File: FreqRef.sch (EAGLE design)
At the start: 33 parts, among them J1 ISP Connector, J2 BNC_RIGHT-ANGLE, SW1 PWR, U1 ATMEGA328, U2 MIC5205, U3 SN74LV164APW

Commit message: Start of Rev-B
Change name to FrequencyReference.
Added part num to BNC connector.
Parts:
- FRAME1: CREVISION Rev A -> Rev B; DATECODE 02SEP2015 -> 2015
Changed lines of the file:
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@@
 <part name="FRAME1" library="NewFrame" deviceset="FRAME_LTR_CU_MARK" device="">
 <attribute name="CNAME" value="Frequency Standard"/>
-<attribute name="CREVISION" value="Rev A"/>
-<attribute name="DATECODE" value="02SEP2015"/>
+<attribute name="CREVISION" value="Rev B"/>
+<attribute name="DATECODE" value="2015"/>
 <attribute name="DESIGNER" value="C.Schnarel"/>
 </part>

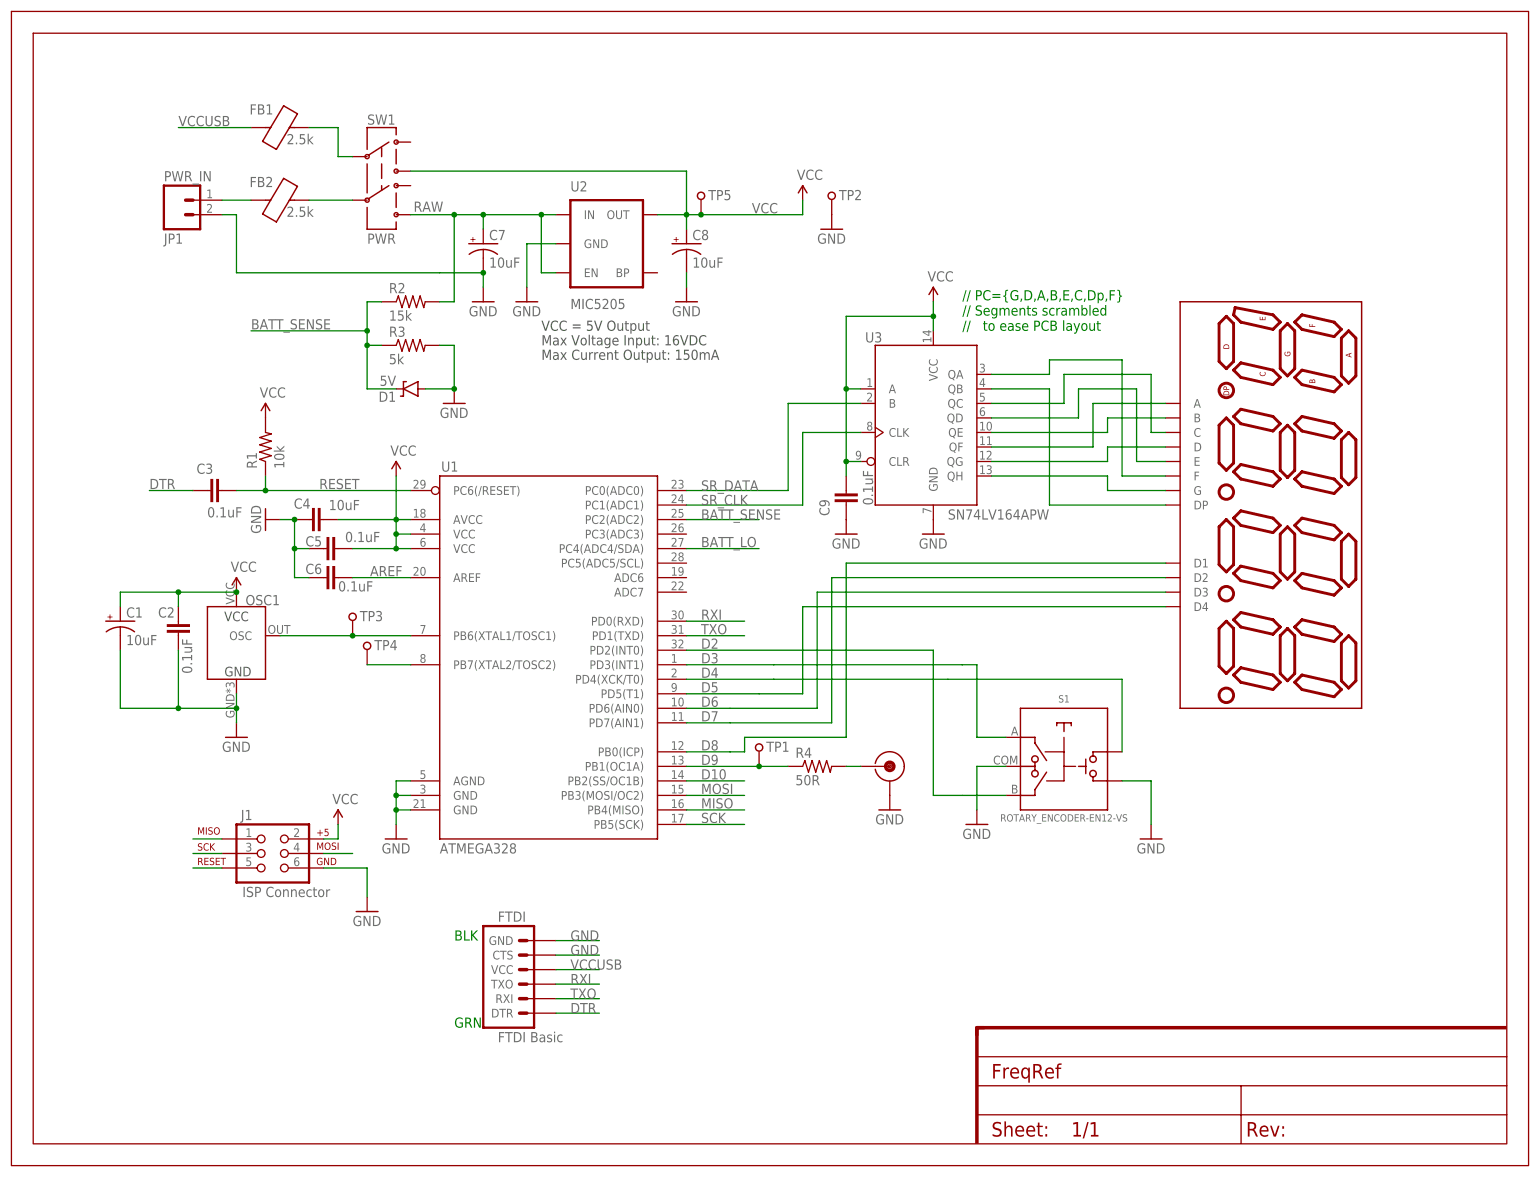
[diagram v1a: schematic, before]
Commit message: More docs. Rev-B layout. Debugged sketch.
Continue documentation. Added two oscillator options to PCB schematic
and layout.  Debugged sketch  on Redboard.
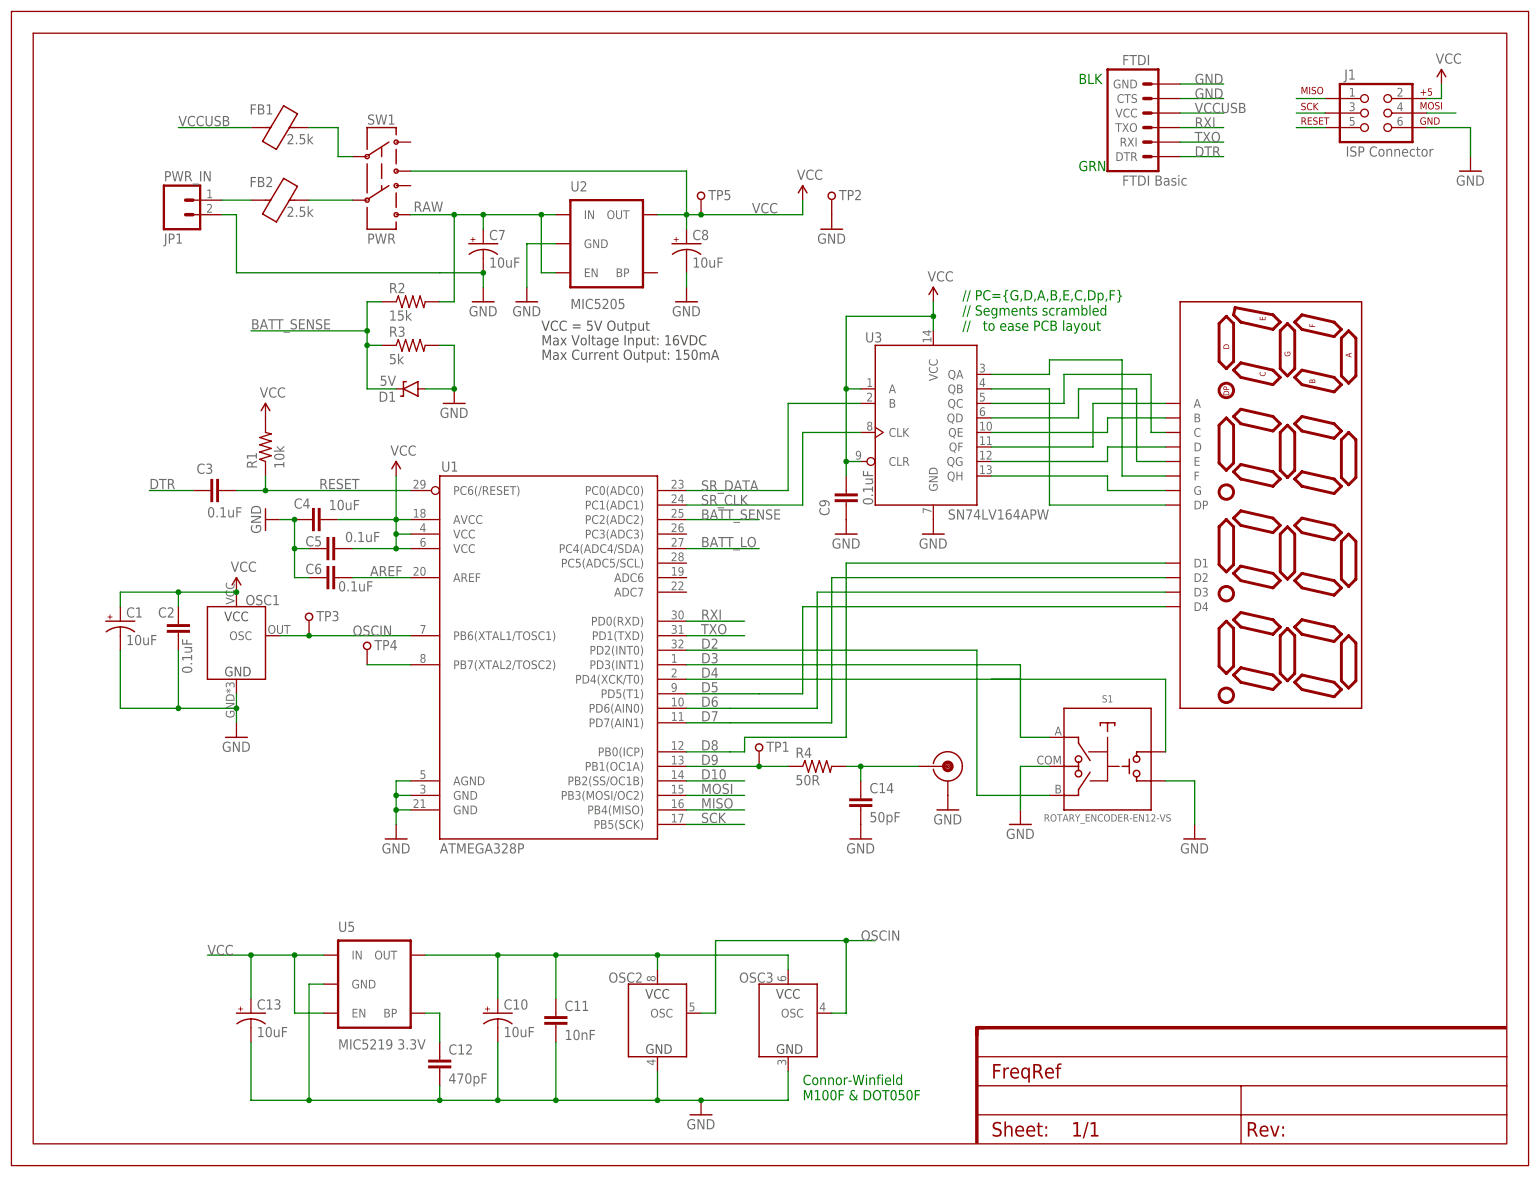
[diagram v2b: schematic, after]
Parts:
- added C10, C13: 10uF, ChipsParts:CAP_POL0805
- added C11: 10nF, SparkFun-Capacitors:CAP0805
- added C12: 470pF, SparkFun-Capacitors:CAP0805
- added C14: 50pF, SparkFun-Capacitors:CAP0805
- added OSC2: (no value), playground:TCXOM100
- added OSC3: (no value), playground:TCXODOT
- added U5: MIC5219 3.3V, SparkFun-PowerIC:V_REG_MIC52193.3V
- FRAME1: CNAME Frequency Standard -> Frequency Reference; CREVISION Rev B -> Rev-B
- OSC1: device playground:TCXO-RTXO230LC -> playground:TCXORALTRON
- U1: value ATMEGA328 -> ATMEGA328P
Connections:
- net N$31 renamed VIN
- removed net N$5: OSC1.OSC, TP3.P$1, U1.PB6(XTAL1/TOSC1)
- new net N$14: C10.+, C11.1, OSC2.VCC, OSC3.VCC, U5.OUT
- new net N$15: C12.1, U5.BP
- new net OSCIN: OSC1.OSC, OSC2.OSC, OSC3.OSC, TP3.P$1, U1.PB6(XTAL1/TOSC1)
- net GND: now also C10.-, C11.2, C12.2, C13.-, C14.2, OSC2.GND, OSC3.GND, U5.GND
- net N$11: now also C14.1
- net VCC: now also C13.+, U5.EN, U5.IN
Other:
- note added: "Connor-Winfield M100F & DOT050F"
- moved on the sheet: FTDI, J1, S1, TP3

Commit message: Software debug.  Schematic values. Added photos.
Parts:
- R2: value 15k -> 10k
- R3: value 5k -> 3.3k
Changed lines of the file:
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@@
 <part name="JP1" library="SparkFun-Connectors" deviceset="M02" device="POLAR" value="PWR_IN"/>
 <part name="SW1" library="StdBxLibrary_BETA_" deviceset="SWITCH,BUTTON,ROUND,7MM" device="" value="PWR"/>
-<part name="R2" library="SparkFun-Resistors" deviceset="RESISTOR" device="0805-RES" value="15k"/>
-<part name="R3" library="SparkFun-Resistors" deviceset="RESISTOR" device="0805-RES" value="5k"/>
+<part name="R2" library="SparkFun-Resistors" deviceset="RESISTOR" device="0805-RES" value="10k"/>
+<part name="R3" library="SparkFun-Resistors" deviceset="RESISTOR" device="0805-RES" value="3.3k"/>
 <part name="GND5" library="SparkFun" deviceset="GND" device=""/>
 <part name="D1" library="SparkFun-DiscreteSemi" deviceset="DIODE-ZENER" device="3.3V" value="5V"/>
